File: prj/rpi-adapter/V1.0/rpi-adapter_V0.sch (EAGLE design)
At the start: 8 parts

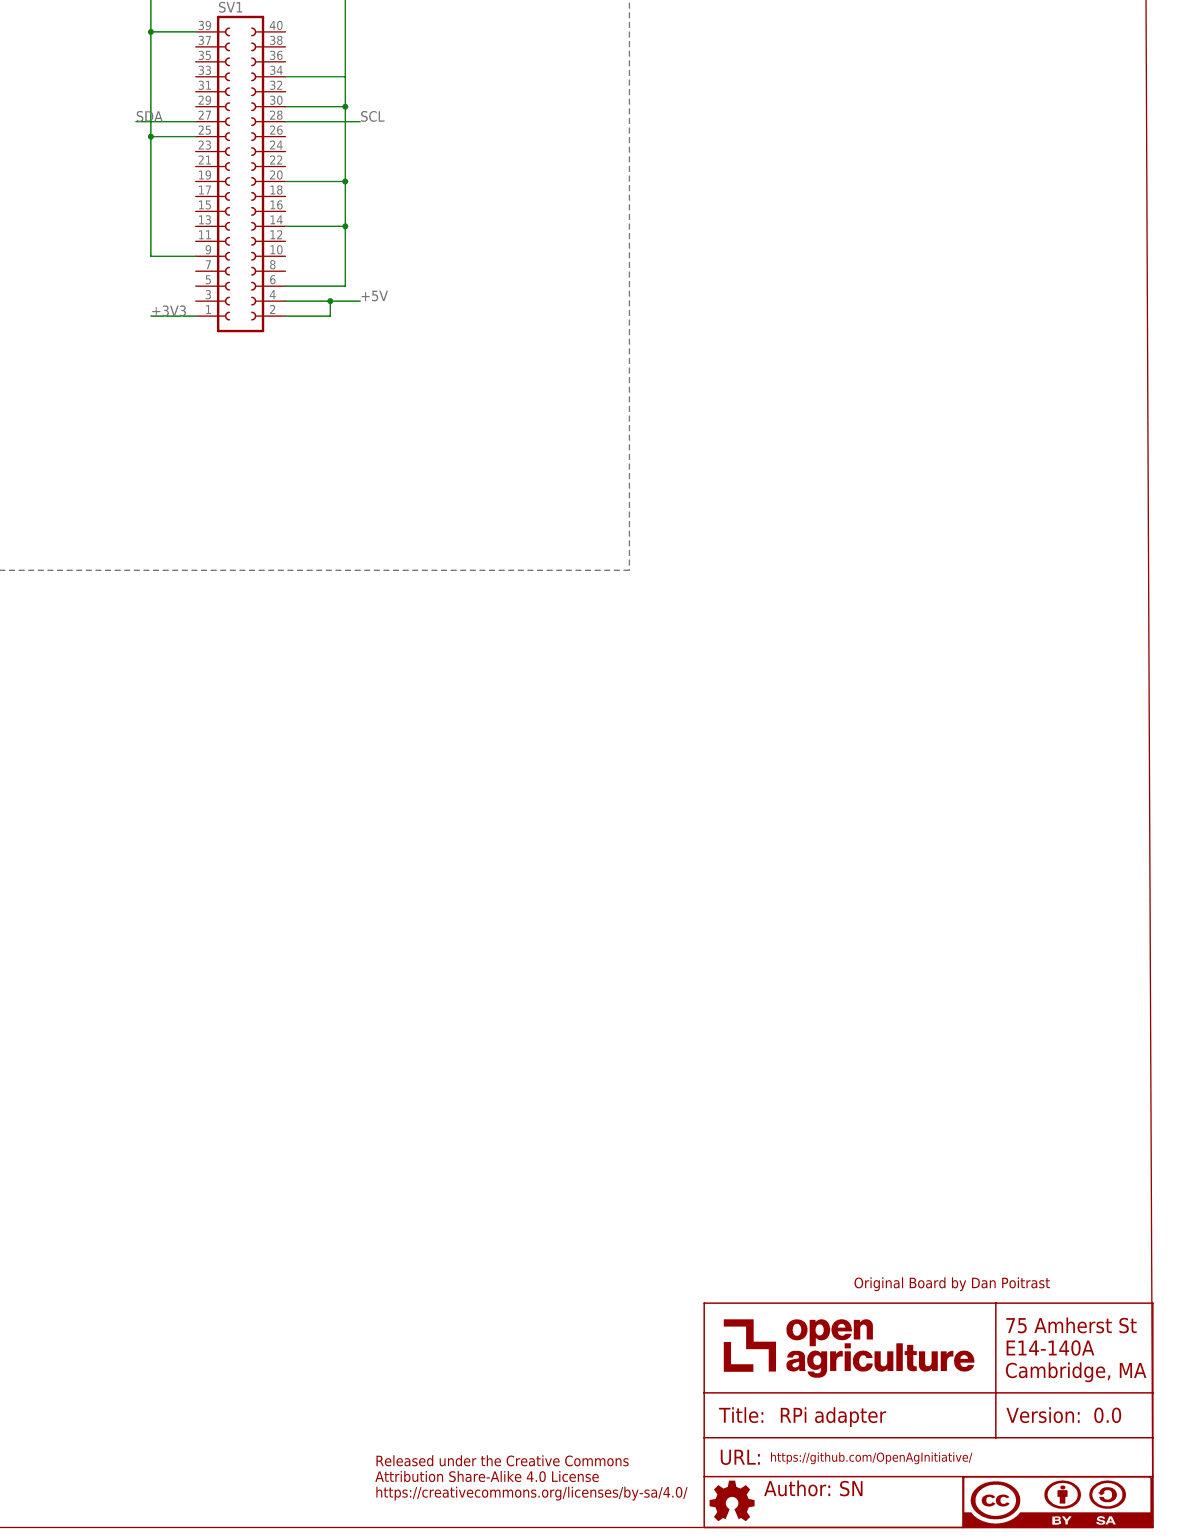
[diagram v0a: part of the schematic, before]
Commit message: Added boards
waterbot board, relay board
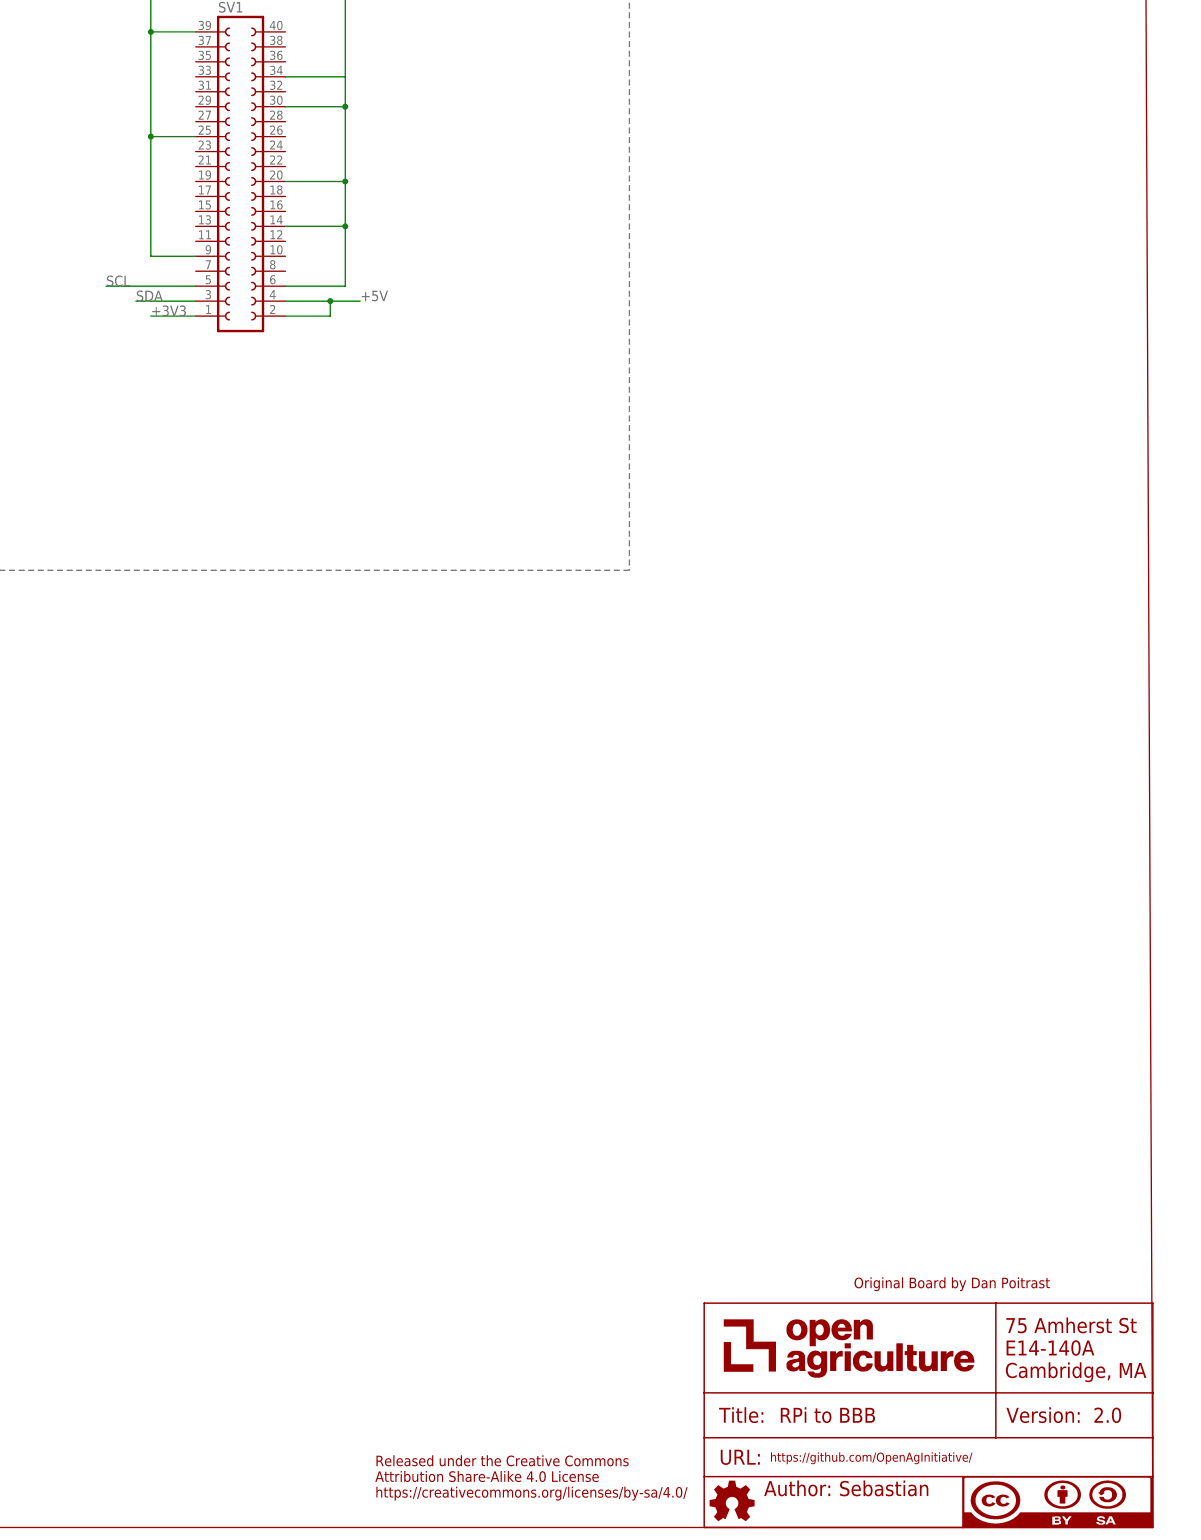
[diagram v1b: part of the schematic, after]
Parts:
- ATTRIBUTES: AUTHOR SN -> Sebastian; DESCRIPTION RPi to BBB adapter -> RPi to BBB; TITLE RPi adapter -> RPi to BBB; VER 0.0 -> 2.0
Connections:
- net SCL: now also SV1.5; no longer SV1.28
- net SDA: now also SV1.3; no longer SV1.27
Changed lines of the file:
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@@
 <parts>
 <part name="ATTRIBUTES" library="openag-frames" deviceset="DOCFIELD" device="">
-<attribute name="AUTHOR" value="SN"/>
-<attribute name="DESCRIPTION" value="RPi to BBB adapter"/>
-<attribute name="TITLE" value="RPi adapter"/>
+<attribute name="AUTHOR" value="Sebastian"/>
+<attribute name="DESCRIPTION" value="RPi to BBB"/>
+<attribute name="TITLE" value="RPi to BBB"/>
 <attribute name="URL" value="https://github.com/OpenAgInitiative/"/>
-<attribute name="VER" value="0.0"/>
+<attribute name="VER" value="2.0"/>
 </part>
 <part name="D2" library="openag-diodes" deviceset="APT1608CGCK" device="" value="APT1608CGCK"/>
@@
 <net name="SDA" class="0">
 <segment>
-<pinref part="SV1" gate="G$1" pin="27"/>
-<wire x1="-162.56" y1="236.22" x2="-172.72" y2="236.22" width="0.1524" layer="91"/>
-<label x="-172.72" y="236.22" size="1.778" layer="95"/>
-</segment>
-<segment>
 <pinref part="SV2" gate="G$1" pin="20"/>
 <wire x1="-279.4" y1="226.06" x2="-271.78" y2="226.06" width="0.1524" layer="91"/>
 <label x="-271.78" y="226.06" size="1.778" layer="95"/>
 </segment>
+<segment>
+<pinref part="SV1" gate="G$1" pin="3"/>
+<wire x1="-162.56" y1="205.74" x2="-172.72" y2="205.74" width="0.1524" layer="91"/>
+<label x="-172.72" y="205.74" size="1.778" layer="95"/>
+</segment>
 </net>
 <net name="SCL" class="0">
-<segment>
-<pinref part="SV1" gate="G$1" pin="28"/>
-<wire x1="-147.32" y1="236.22" x2="-134.62" y2="236.22" width="0.1524" layer="91"/>
-<label x="-134.62" y="236.22" size="1.778" layer="95"/>
-</segment>
 <segment>
 <pinref part="SV2" gate="G$1" pin="19"/>
@@
 <label x="-302.26" y="226.06" size="1.778" layer="95"/>
 </segment>
-</net>
+<segment>
+<pinref part="SV1" gate="G$1" pin="5"/>
+<wire x1="-162.56" y1="208.28" x2="-177.8" y2="208.28" width="0.1524" layer="91"/>
+<label x="-177.8" y="208.28" size="1.778" layer="95"/>
+</segment>
+</net>
